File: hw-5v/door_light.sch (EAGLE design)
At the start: 36 parts, among them IC1 TINY13-20SSU, Q1 BSP250, T1 IRFML8244, T2 KP-3216P3C, T3 IRFML8244, U1 MC33063ADE4

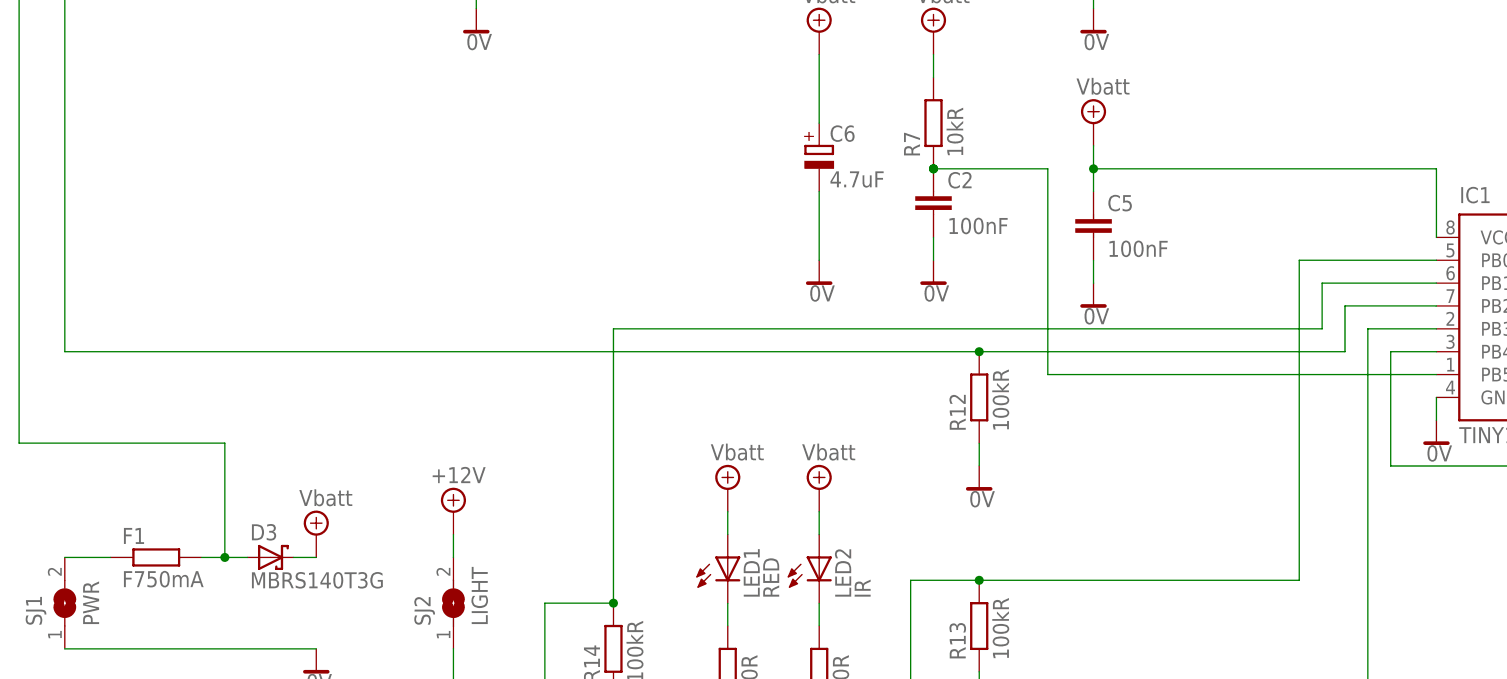
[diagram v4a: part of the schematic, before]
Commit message: fixed BSP250's pull-down to be a pull-up (10kR)
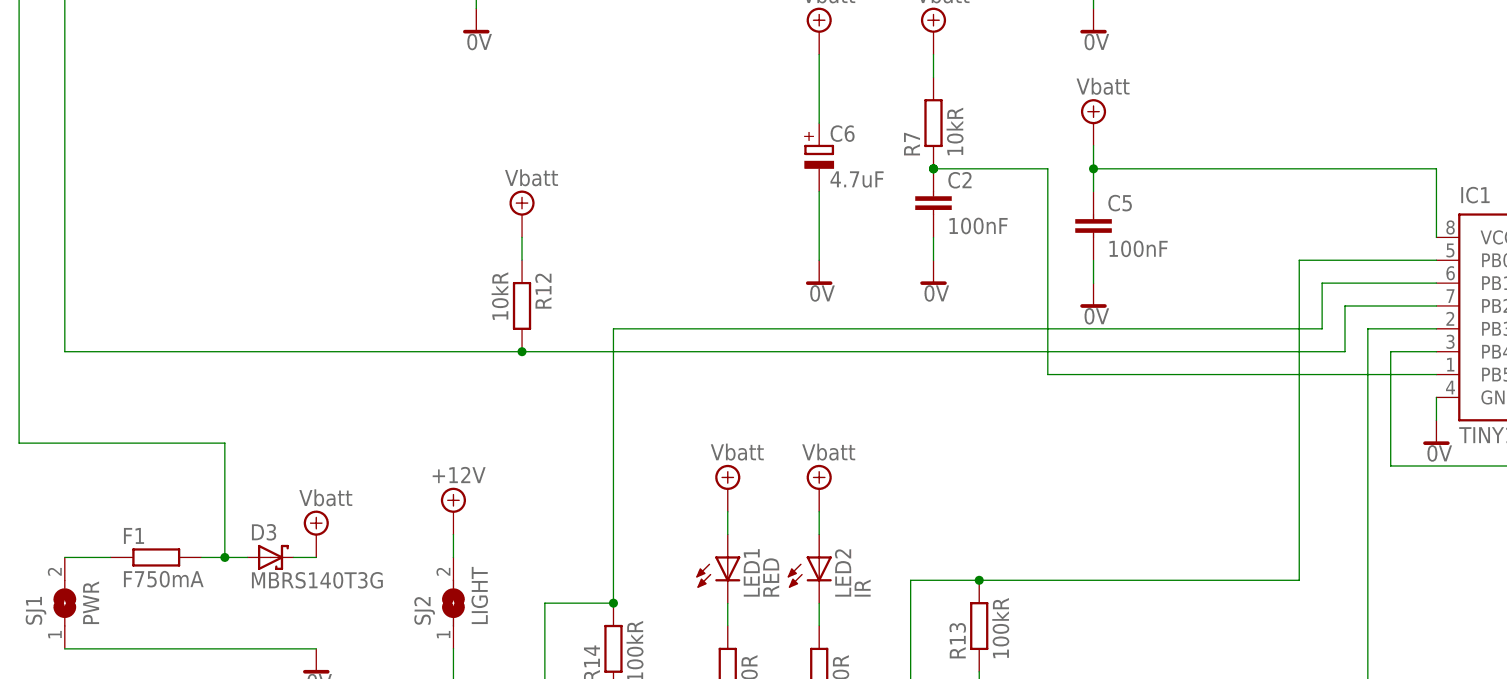
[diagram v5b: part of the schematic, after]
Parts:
- R12: value 100kR -> 10kR
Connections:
- net +4.1V: now also R12.1
- net 0V: no longer R12.1
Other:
- moved on the sheet: R12
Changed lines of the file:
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@@
 <part name="SJ1" library="jumper" deviceset="SJ" device="W" value="PWR"/>
 <part name="SJ2" library="jumper" deviceset="SJ" device="W" value="LIGHT"/>
-<part name="R12" library="rcl" deviceset="R-EU_" device="R0603" value="100kR"/>
+<part name="R12" library="rcl" deviceset="R-EU_" device="R0603" value="10kR"/>
 <part name="R13" library="rcl" deviceset="R-EU_" device="R0603" value="100kR"/>
-<part name="SUPPLY15" library="supply2" deviceset="0V" device=""/>
 <part name="SUPPLY16" library="supply2" deviceset="0V" device=""/>
 <part name="D2" library="diode" deviceset="MBRS130LT3" device="" value=" MBRS140T3G"/>
@@
 <part name="R14" library="rcl" deviceset="R-EU_" device="R0603" value="100kR"/>
 <part name="SUPPLY31" library="supply2" deviceset="0V" device=""/>
+<part name="SUPPLY7" library="supply2" deviceset="+4.1V" device="" value="Vbatt"/>
 </parts>
 <sheets>
@@
 <instance part="SJ1" gate="1" x="-53.34" y="35.56" rot="R90"/>
 <instance part="SJ2" gate="1" x="-10.16" y="35.56" rot="R90"/>
-<instance part="R12" gate="G$1" x="48.26" y="58.42" rot="R90"/>
+<instance part="R12" gate="G$1" x="-2.54" y="68.58" rot="R270"/>
 <instance part="R13" gate="G$1" x="48.26" y="33.02" rot="R90"/>
-<instance part="SUPPLY15" gate="0V" x="48.26" y="48.26"/>
 <instance part="SUPPLY16" gate="0V" x="48.26" y="22.86"/>
 <instance part="D2" gate="G$1" x="-53.34" y="152.4"/>
@@
 <instance part="R14" gate="G$1" x="7.62" y="30.48" rot="R90"/>
 <instance part="SUPPLY31" gate="0V" x="7.62" y="10.16"/>
+<instance part="SUPPLY7" gate="P" x="-2.54" y="78.74"/>
 </instances>
 <busses>
@@
 <pinref part="SUPPLY14" gate="0V" pin="0V"/>
 <wire x1="-25.4" y1="30.48" x2="-53.34" y2="30.48" width="0.1524" layer="91"/>
-</segment>
-<segment>
-<pinref part="R12" gate="G$1" pin="1"/>
-<pinref part="SUPPLY15" gate="0V" pin="0V"/>
-<wire x1="48.26" y1="50.8" x2="48.26" y2="53.34" width="0.1524" layer="91"/>
 </segment>
 <segment>
@@
 <wire x1="-40.64" y1="147.32" x2="-53.34" y2="147.32" width="0.1524" layer="91"/>
 <wire x1="-53.34" y1="147.32" x2="-53.34" y2="63.5" width="0.1524" layer="91"/>
-<wire x1="-53.34" y1="63.5" x2="48.26" y2="63.5" width="0.1524" layer="91"/>
-<wire x1="48.26" y1="63.5" x2="88.9" y2="63.5" width="0.1524" layer="91"/>
+<wire x1="-53.34" y1="63.5" x2="-2.54" y2="63.5" width="0.1524" layer="91"/>
+<wire x1="-2.54" y1="63.5" x2="88.9" y2="63.5" width="0.1524" layer="91"/>
 <wire x1="88.9" y1="63.5" x2="88.9" y2="68.58" width="0.1524" layer="91"/>
 <pinref part="Q1" gate="G$1" pin="G"/>
 <pinref part="R12" gate="G$1" pin="2"/>
-<junction x="48.26" y="63.5"/>
+<junction x="-2.54" y="63.5"/>
 <pinref part="IC1" gate="G$1" pin="PB2/PCINT2/SCK/ADC1/T0"/>
 <wire x1="99.06" y1="68.58" x2="88.9" y2="68.58" width="0.1524" layer="91"/>
@@
 <wire x1="30.48" y1="96.52" x2="30.48" y2="88.9" width="0.1524" layer="91"/>
 </segment>
-</net>
+<segment>
+<pinref part="R12" gate="G$1" pin="1"/>
+<pinref part="SUPPLY7" gate="P" pin="+4.1V"/>
+<wire x1="-2.54" y1="76.2" x2="-2.54" y2="73.66" width="0.1524" layer="91"/>
+</segment>
+</net>

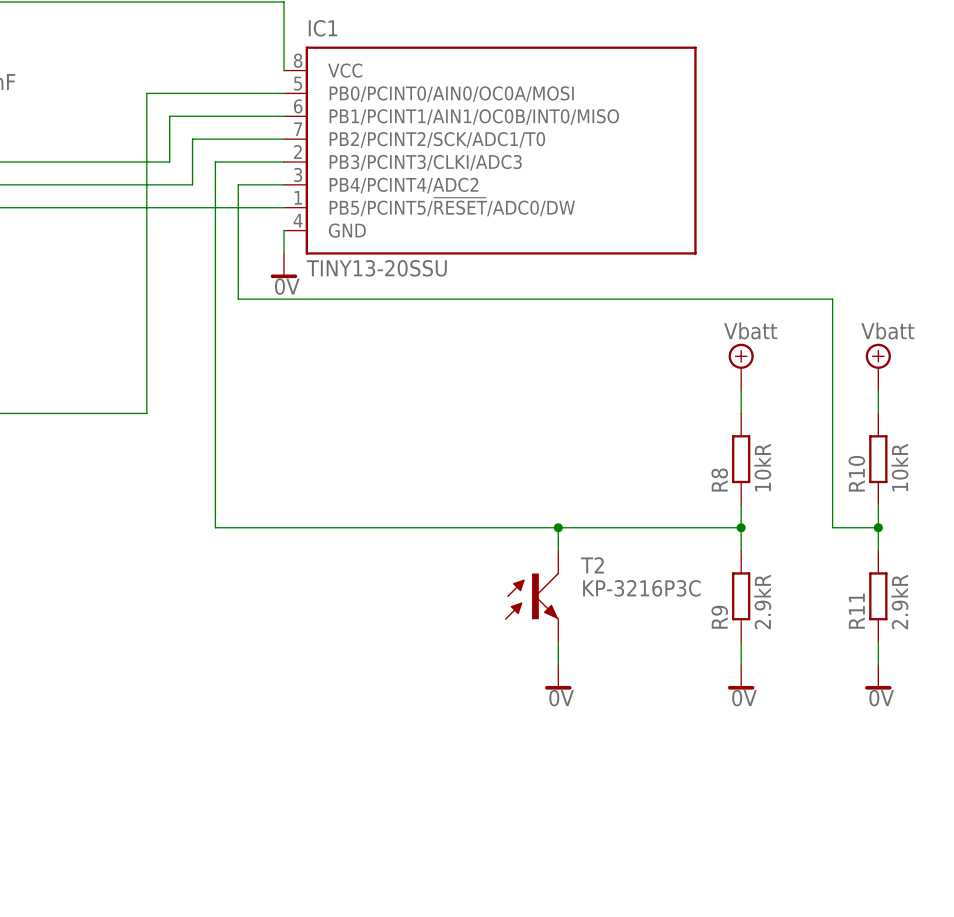
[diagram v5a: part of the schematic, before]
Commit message: added -3V zenner for ensuring reasonable measurements of IR light change
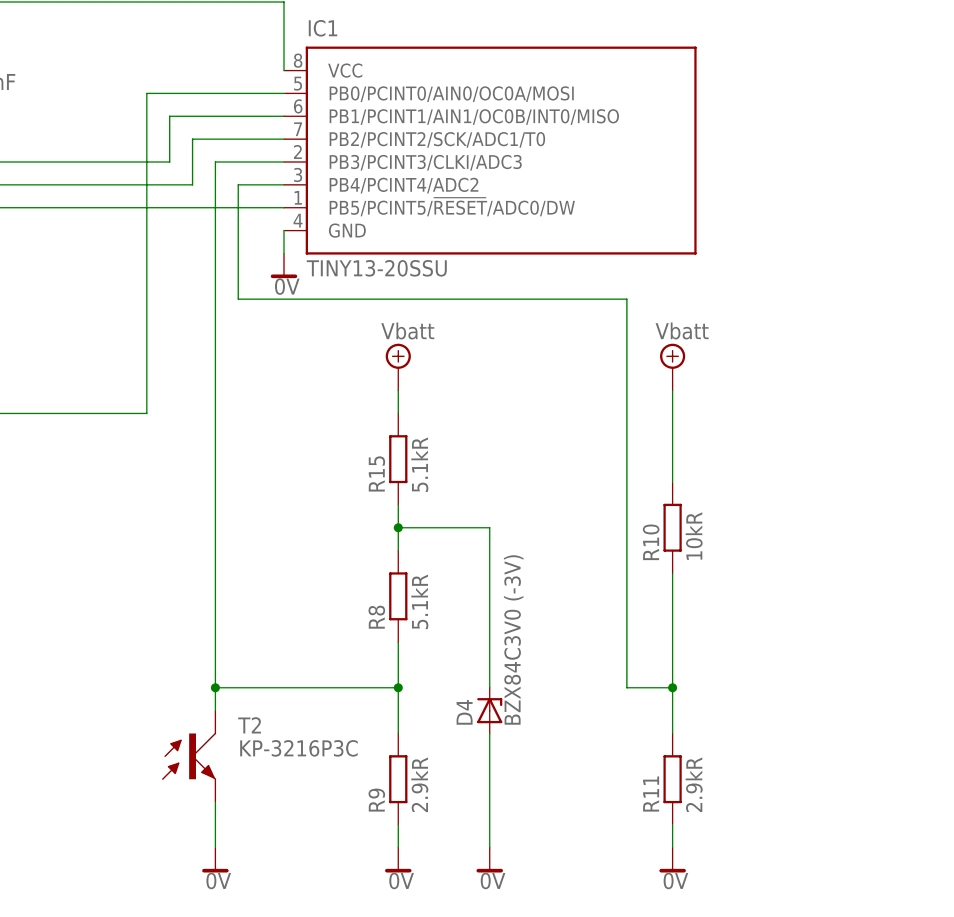
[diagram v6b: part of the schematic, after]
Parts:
- added D4: BZX84C3V0 (-3V), diode:BZX84CSMD
- added R15: 5.1kR, rcl:R-EU_R0603
- R8: value 10kR -> 5.1kR
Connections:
- new net N$6: D4.C, R15.1, R8.2
- net +4.1V: now also R15.2; no longer R8.2
- net 0V: now also D4.A
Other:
- moved on the sheet: R10, R11, R8, R9, T2
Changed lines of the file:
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@@
 <part name="R9" library="rcl" deviceset="R-EU_" device="R0603" value="2.9kR"/>
 <part name="R10" library="rcl" deviceset="R-EU_" device="R0603" value="10kR"/>
-<part name="R8" library="rcl" deviceset="R-EU_" device="R0603" value="10kR"/>
+<part name="R8" library="rcl" deviceset="R-EU_" device="R0603" value="5.1kR"/>
 <part name="R11" library="rcl" deviceset="R-EU_" device="R0603" value="2.9kR"/>
 <part name="SUPPLY22" library="supply2" deviceset="+4.1V" device="" value="Vbatt"/>
@@
 <part name="SUPPLY31" library="supply2" deviceset="0V" device=""/>
 <part name="SUPPLY7" library="supply2" deviceset="+4.1V" device="" value="Vbatt"/>
+<part name="D4" library="diode" deviceset="BZX84CSMD" device="" value="BZX84C3V0 (-3V)"/>
+<part name="R15" library="rcl" deviceset="R-EU_" device="R0603" value="5.1kR"/>
+<part name="SUPPLY15" library="supply2" deviceset="0V" device=""/>
 </parts>
 <sheets>
@@
 <instance part="SUPPLY18" gate="P" x="43.18" y="99.06"/>
 <instance part="SUPPLY1" gate="P" x="60.96" y="88.9"/>
-<instance part="R9" gate="G$1" x="149.86" y="17.78" rot="R90"/>
-<instance part="R10" gate="G$1" x="165.1" y="33.02" rot="R90"/>
-<instance part="R8" gate="G$1" x="149.86" y="33.02" rot="R90"/>
-<instance part="R11" gate="G$1" x="165.1" y="17.78" rot="R90"/>
-<instance part="SUPPLY22" gate="P" x="149.86" y="43.18"/>
-<instance part="SUPPLY23" gate="P" x="165.1" y="43.18"/>
-<instance part="SUPPLY24" gate="0V" x="149.86" y="7.62"/>
-<instance part="SUPPLY25" gate="0V" x="165.1" y="7.62"/>
+<instance part="R9" gate="G$1" x="111.76" y="-2.54" rot="R90"/>
+<instance part="R10" gate="G$1" x="142.24" y="25.4" rot="R90"/>
+<instance part="R8" gate="G$1" x="111.76" y="17.78" rot="R90"/>
+<instance part="R11" gate="G$1" x="142.24" y="-2.54" rot="R90"/>
+<instance part="SUPPLY22" gate="P" x="111.76" y="43.18"/>
+<instance part="SUPPLY23" gate="P" x="142.24" y="43.18"/>
+<instance part="SUPPLY24" gate="0V" x="111.76" y="-12.7"/>
+<instance part="SUPPLY25" gate="0V" x="142.24" y="-12.7"/>
 <instance part="LED2" gate="G$1" x="30.48" y="40.64"/>
 <instance part="LED1" gate="G$1" x="20.32" y="40.64"/>
@@
 <instance part="SUPPLY9" gate="P" x="20.32" y="48.26"/>
 <instance part="SUPPLY27" gate="P" x="30.48" y="48.26"/>
-<instance part="T2" gate="1" x="127" y="17.78"/>
-<instance part="SUPPLY28" gate="0V" x="129.54" y="7.62"/>
+<instance part="T2" gate="1" x="88.9" y="0"/>
+<instance part="SUPPLY28" gate="0V" x="91.44" y="-12.7"/>
 <instance part="Q1" gate="G$1" x="-38.1" y="144.78"/>
 <instance part="T1" gate="A" x="30.48" y="15.24" rot="MR0"/>
@@
 <instance part="SUPPLY31" gate="0V" x="7.62" y="10.16"/>
 <instance part="SUPPLY7" gate="P" x="-2.54" y="78.74"/>
+<instance part="D4" gate="G$1" x="121.92" y="5.08" rot="R90"/>
+<instance part="R15" gate="G$1" x="111.76" y="33.02" rot="R90"/>
+<instance part="SUPPLY15" gate="0V" x="121.92" y="-12.7"/>
 </instances>
 <busses>
@@
 <pinref part="R9" gate="G$1" pin="1"/>
 <pinref part="SUPPLY24" gate="0V" pin="0V"/>
-<wire x1="149.86" y1="10.16" x2="149.86" y2="12.7" width="0.1524" layer="91"/>
+<wire x1="111.76" y1="-10.16" x2="111.76" y2="-7.62" width="0.1524" layer="91"/>
 </segment>
 <segment>
 <pinref part="R11" gate="G$1" pin="1"/>
 <pinref part="SUPPLY25" gate="0V" pin="0V"/>
-<wire x1="165.1" y1="10.16" x2="165.1" y2="12.7" width="0.1524" layer="91"/>
+<wire x1="142.24" y1="-10.16" x2="142.24" y2="-7.62" width="0.1524" layer="91"/>
 </segment>
 <segment>
 <pinref part="T2" gate="1" pin="E"/>
 <pinref part="SUPPLY28" gate="0V" pin="0V"/>
-<wire x1="129.54" y1="12.7" x2="129.54" y2="10.16" width="0.1524" layer="91"/>
+<wire x1="91.44" y1="-5.08" x2="91.44" y2="-10.16" width="0.1524" layer="91"/>
 </segment>
 <segment>
@@
 <pinref part="R14" gate="G$1" pin="1"/>
 <wire x1="7.62" y1="25.4" x2="7.62" y2="12.7" width="0.1524" layer="91"/>
+</segment>
+<segment>
+<pinref part="D4" gate="G$1" pin="A"/>
+<pinref part="SUPPLY15" gate="0V" pin="0V"/>
+<wire x1="121.92" y1="-10.16" x2="121.92" y2="2.54" width="0.1524" layer="91"/>
 </segment>
 </net>
@@
 </segment>
 <segment>
-<pinref part="R8" gate="G$1" pin="2"/>
-<pinref part="SUPPLY22" gate="P" pin="+4.1V"/>
-<wire x1="149.86" y1="40.64" x2="149.86" y2="38.1" width="0.1524" layer="91"/>
-</segment>
-<segment>
 <pinref part="R10" gate="G$1" pin="2"/>
 <pinref part="SUPPLY23" gate="P" pin="+4.1V"/>
-<wire x1="165.1" y1="40.64" x2="165.1" y2="38.1" width="0.1524" layer="91"/>
+<wire x1="142.24" y1="40.64" x2="142.24" y2="30.48" width="0.1524" layer="91"/>
 </segment>
 <segment>
@@
 <pinref part="SUPPLY7" gate="P" pin="+4.1V"/>
 <wire x1="-2.54" y1="76.2" x2="-2.54" y2="73.66" width="0.1524" layer="91"/>
+</segment>
+<segment>
+<pinref part="SUPPLY22" gate="P" pin="+4.1V"/>
+<pinref part="R15" gate="G$1" pin="2"/>
+<wire x1="111.76" y1="38.1" x2="111.76" y2="40.64" width="0.1524" layer="91"/>
 </segment>
 </net>
@@
 <pinref part="R8" gate="G$1" pin="1"/>
 <pinref part="R9" gate="G$1" pin="2"/>
-<wire x1="149.86" y1="22.86" x2="149.86" y2="25.4" width="0.1524" layer="91"/>
-<wire x1="149.86" y1="25.4" x2="149.86" y2="27.94" width="0.1524" layer="91"/>
-<wire x1="149.86" y1="25.4" x2="129.54" y2="25.4" width="0.1524" layer="91"/>
-<wire x1="129.54" y1="25.4" x2="91.44" y2="25.4" width="0.1524" layer="91"/>
-<wire x1="91.44" y1="25.4" x2="91.44" y2="66.04" width="0.1524" layer="91"/>
+<wire x1="111.76" y1="2.54" x2="111.76" y2="7.62" width="0.1524" layer="91"/>
+<wire x1="111.76" y1="7.62" x2="111.76" y2="12.7" width="0.1524" layer="91"/>
+<wire x1="111.76" y1="7.62" x2="91.44" y2="7.62" width="0.1524" layer="91"/>
+<wire x1="91.44" y1="7.62" x2="91.44" y2="66.04" width="0.1524" layer="91"/>
 <pinref part="IC1" gate="G$1" pin="PB3/PCINT3/CLKI/ADC3"/>
 <wire x1="91.44" y1="66.04" x2="99.06" y2="66.04" width="0.1524" layer="91"/>
-<junction x="149.86" y="25.4"/>
+<junction x="111.76" y="7.62"/>
 <pinref part="T2" gate="1" pin="C"/>
-<wire x1="129.54" y1="22.86" x2="129.54" y2="25.4" width="0.1524" layer="91"/>
-<junction x="129.54" y="25.4"/>
+<wire x1="91.44" y1="5.08" x2="91.44" y2="7.62" width="0.1524" layer="91"/>
+<junction x="91.44" y="7.62"/>
 </segment>
 </net>
@@
 <pinref part="R10" gate="G$1" pin="1"/>
 <pinref part="R11" gate="G$1" pin="2"/>
-<wire x1="165.1" y1="22.86" x2="165.1" y2="25.4" width="0.1524" layer="91"/>
-<wire x1="165.1" y1="25.4" x2="165.1" y2="27.94" width="0.1524" layer="91"/>
-<wire x1="165.1" y1="25.4" x2="160.02" y2="25.4" width="0.1524" layer="91"/>
-<wire x1="160.02" y1="25.4" x2="160.02" y2="50.8" width="0.1524" layer="91"/>
-<wire x1="160.02" y1="50.8" x2="93.98" y2="50.8" width="0.1524" layer="91"/>
+<wire x1="142.24" y1="2.54" x2="142.24" y2="7.62" width="0.1524" layer="91"/>
+<wire x1="142.24" y1="7.62" x2="142.24" y2="20.32" width="0.1524" layer="91"/>
+<wire x1="142.24" y1="7.62" x2="137.16" y2="7.62" width="0.1524" layer="91"/>
+<wire x1="137.16" y1="7.62" x2="137.16" y2="50.8" width="0.1524" layer="91"/>
+<wire x1="137.16" y1="50.8" x2="93.98" y2="50.8" width="0.1524" layer="91"/>
 <wire x1="93.98" y1="50.8" x2="93.98" y2="63.5" width="0.1524" layer="91"/>
 <pinref part="IC1" gate="G$1" pin="PB4/PCINT4/ADC2"/>
 <wire x1="93.98" y1="63.5" x2="99.06" y2="63.5" width="0.1524" layer="91"/>
-<junction x="165.1" y="25.4"/>
+<junction x="142.24" y="7.62"/>
 </segment>
 </net>
@@
 </segment>
 </net>
+<net name="N$6" class="0">
+<segment>
+<pinref part="R8" gate="G$1" pin="2"/>
+<pinref part="R15" gate="G$1" pin="1"/>
+<wire x1="111.76" y1="27.94" x2="111.76" y2="25.4" width="0.1524" layer="91"/>
+<pinref part="D4" gate="G$1" pin="C"/>
+<wire x1="111.76" y1="25.4" x2="111.76" y2="22.86" width="0.1524" layer="91"/>
+<wire x1="111.76" y1="25.4" x2="121.92" y2="25.4" width="0.1524" layer="91"/>
+<wire x1="121.92" y1="25.4" x2="121.92" y2="7.62" width="0.1524" layer="91"/>
+<junction x="111.76" y="25.4"/>
+</segment>
+</net>
